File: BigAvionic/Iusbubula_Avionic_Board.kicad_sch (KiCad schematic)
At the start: 136 parts, among them J1 Conn_01x02, J10 Conn_01x04, J12 Conn_01x04, J2 USB_C_Receptacle_USB2.0_16P, J3 Conn_01x04, J5 Conn_01x02, J6 Micro_SD_Card_Det1, J7 Screw_Terminal_01x01, J9 Conn_01x04, Q1 TSM3481CX6 RFG, Q2 TSM3481CX6 RFG, Q5 NMOS, SW1 SW_Push, SW2 USER_Buttom, SW3 USER_Buttom, U1 STM32F405VGTx, U10 E22-400T30S, U11 E80-900M23313S, U12 W25Q128JVS, U2 LD1117S33TR_SOT223, U3 LTC4412xS6, U4 TPS54538RQFR, U5 BMI088, U6 BMP390, U8 ADXL375BCCZ, Y1 8Mhz

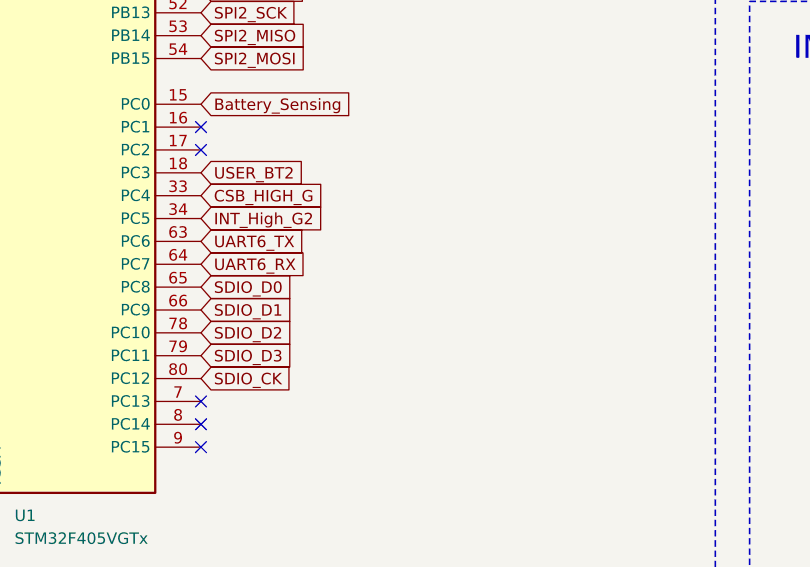
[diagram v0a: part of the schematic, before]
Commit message: adjust top layer wiring
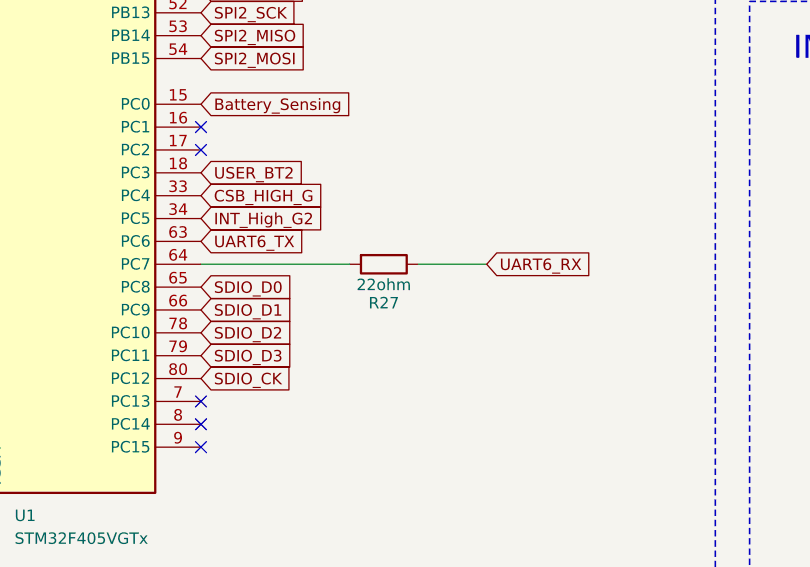
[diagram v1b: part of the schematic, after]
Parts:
- added R27: 22ohm, Resistor_SMD:R_0805_2012Metric_Pad1.20x1.40mm_HandSolder, symbol Device:R
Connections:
- net UART6_RX: now also R27.1; no longer U1.64 (PC7)
- new net: R27.2, U1.64 (PC7)
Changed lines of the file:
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@@
 	(wire
 		(pts
+			(xy 165.1 167.64) (xy 148.59 167.64)
+		)
+		(stroke
+			(width 0)
+			(type default)
+		)
+	)
+	(wire
+		(pts
 			(xy 91.44 240.03) (xy 91.44 243.84)
 		)
@@
 	(wire
 		(pts
+			(xy 180.34 167.64) (xy 172.72 167.64)
+		)
+		(stroke
+			(width 0)
+			(type default)
+		)
+	)
+	(wire
+		(pts
 			(xy 316.23 111.76) (xy 316.23 113.03)
 		)
@@
 	(global_label "UART6_RX"
 		(shape input)
-		(at 148.59 167.64 0)
+		(at 180.34 167.64 0)
 		(fields_autoplaced yes)
 		(effects
@@
 		)
 		(property "Intersheetrefs" "${INTERSHEET_REFS}"
-			(at 160.8885 167.64 0)
+			(at 192.6385 167.64 0)
 			(effects
 				(font
@@
 					(unit 1)
 				)
+			)
+		)
+	)
+	(symbol
+		(lib_id "Device:R")
+		(at 168.91 167.64 270)
+		(unit 1)
+		(exclude_from_sim no)
+		(in_bom yes)
+		(on_board yes)
+		(dnp no)
+		(property "Reference" "R27"
+			(at 168.91 171.958 90)
+			(effects
+				(font
+					(size 1.27 1.27)
+				)
+			)
+		)
+		(property "Value" "22ohm"
+			(at 168.91 169.926 90)
+			(effects
+				(font
+					(size 1.27 1.27)
+				)
+			)
+		)
+		(property "Footprint" "Resistor_SMD:R_0805_2012Metric_Pad1.20x1.40mm_HandSolder"
+			(at 168.91 165.862 90)
+			(effects
+				(font
+					(size 1.27 1.27)
+				)
+				(hide yes)
+			)
+		)
+		(property "Datasheet" "~"
+			(at 168.91 167.64 0)
+			(effects
+				(font
+					(size 1.27 1.27)
+				)
+				(hide yes)
+			)
+		)
+		(property "Description" "Resistor"
+			(at 168.91 167.64 0)
+			(effects
+				(font
+					(size 1.27 1.27)
+				)
+				(hide yes)
+			)
+		)
+		(pin "1"
+		)
+		(pin "2"
+		)
+		(instances
+			(project "Iusbubula_Avionic_Board"
+				(path "/80a059dc-2311-4dd3-afad-18a5367fc218"
+					(reference "R27")
+					(unit 1)
+				)
